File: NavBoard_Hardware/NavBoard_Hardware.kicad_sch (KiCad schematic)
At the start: 0 parts

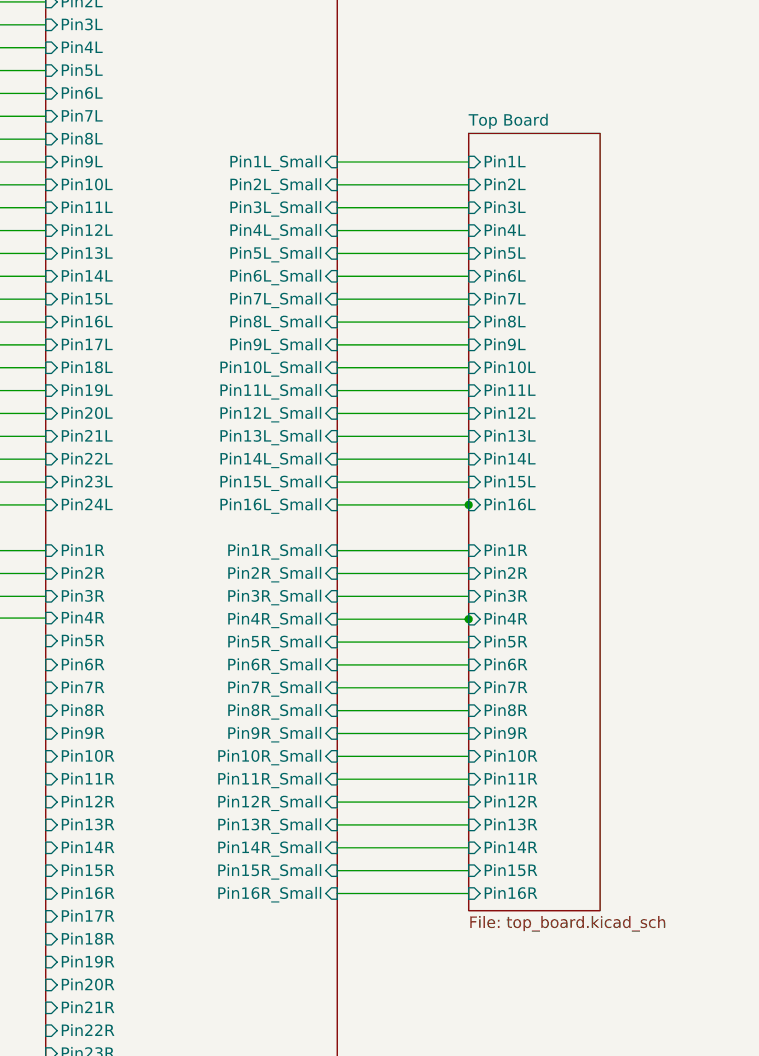
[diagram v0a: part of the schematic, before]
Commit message: Created adapter symbols and footprints
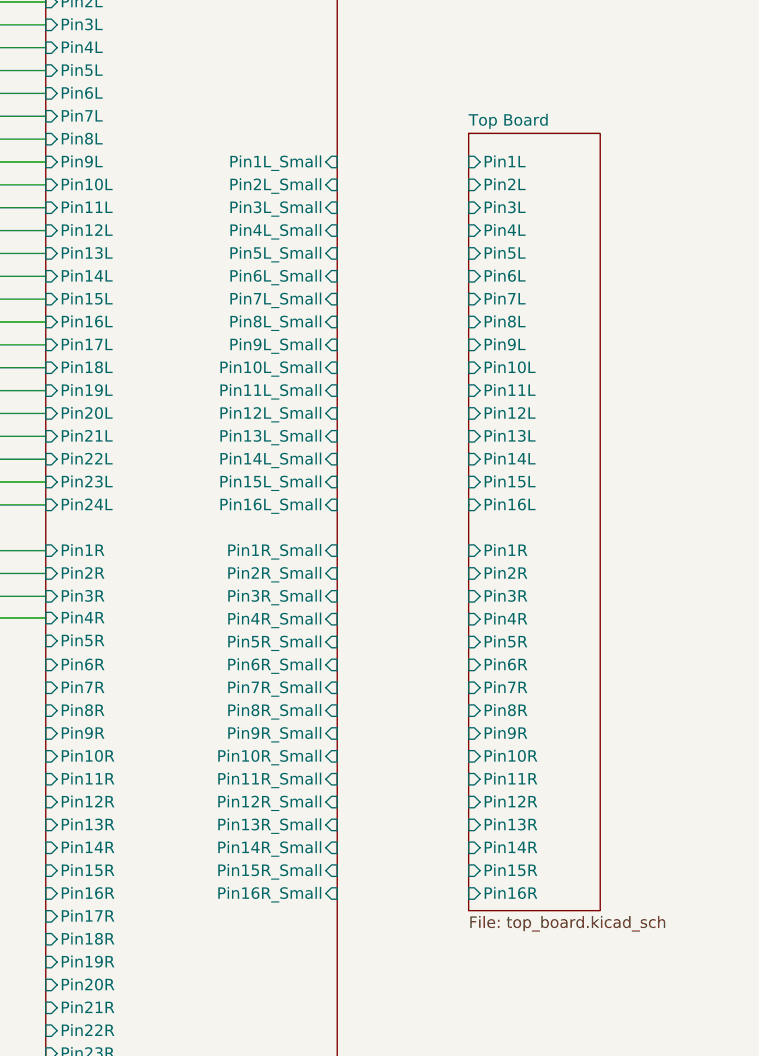
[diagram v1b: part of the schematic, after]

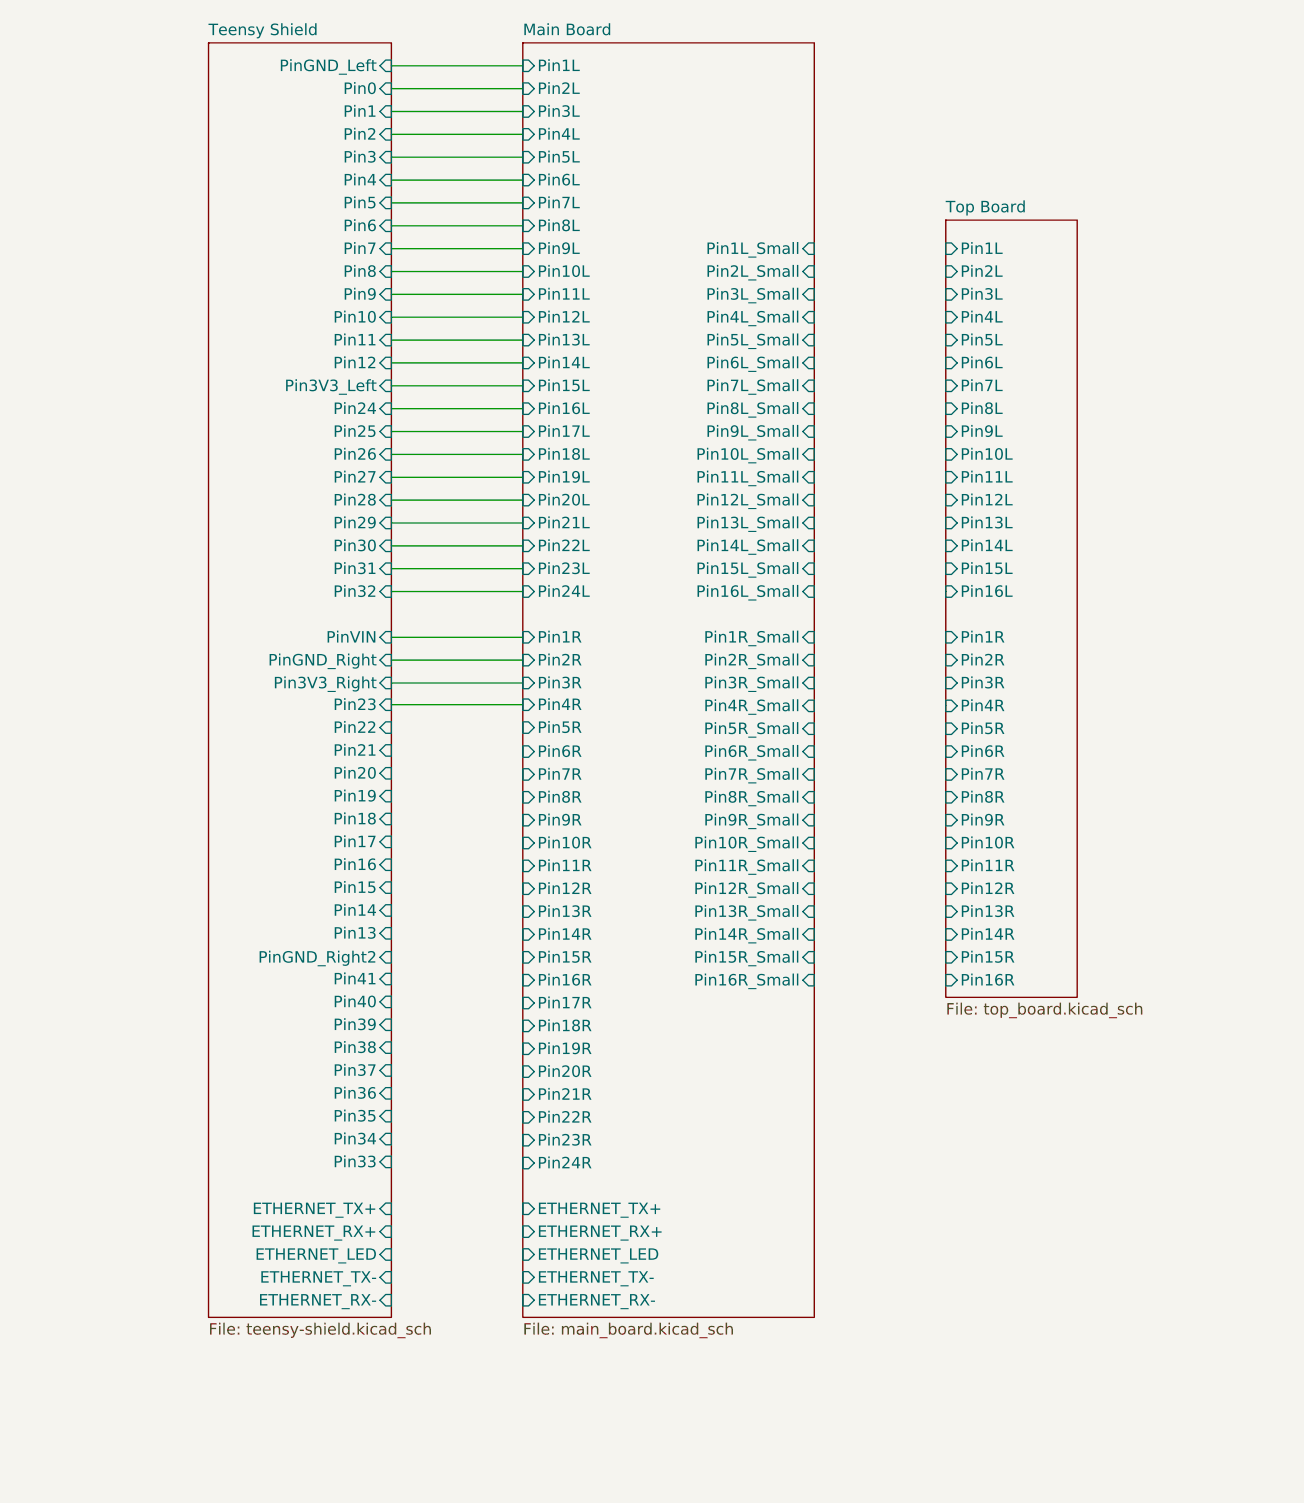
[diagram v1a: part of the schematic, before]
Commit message: Added connectors, cleaned up file directory
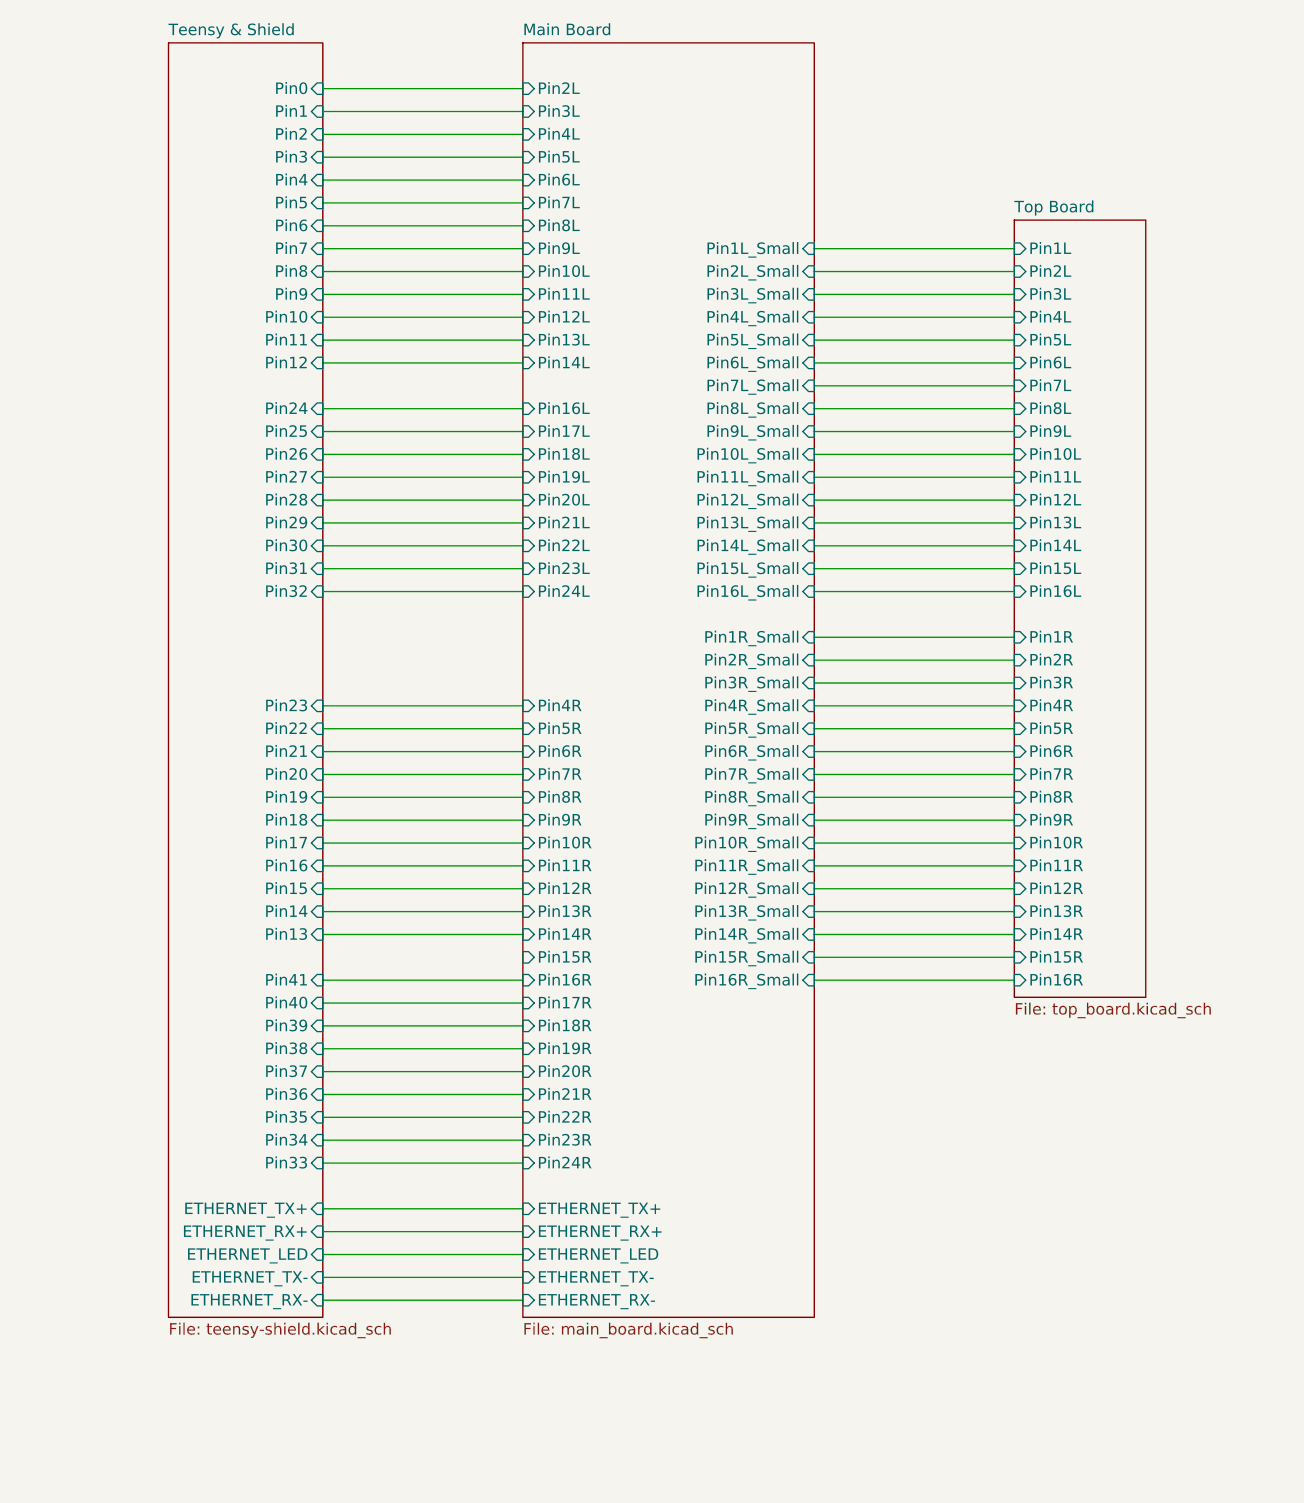
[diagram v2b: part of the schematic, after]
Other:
- removed sheet Teensy Shield
- added sheet Teensy & Shield (teensy-shield.kicad_sch)
- sheet Main Board ports: added none; removed Pin15L, Pin1L, Pin1R, Pin2R, Pin3R

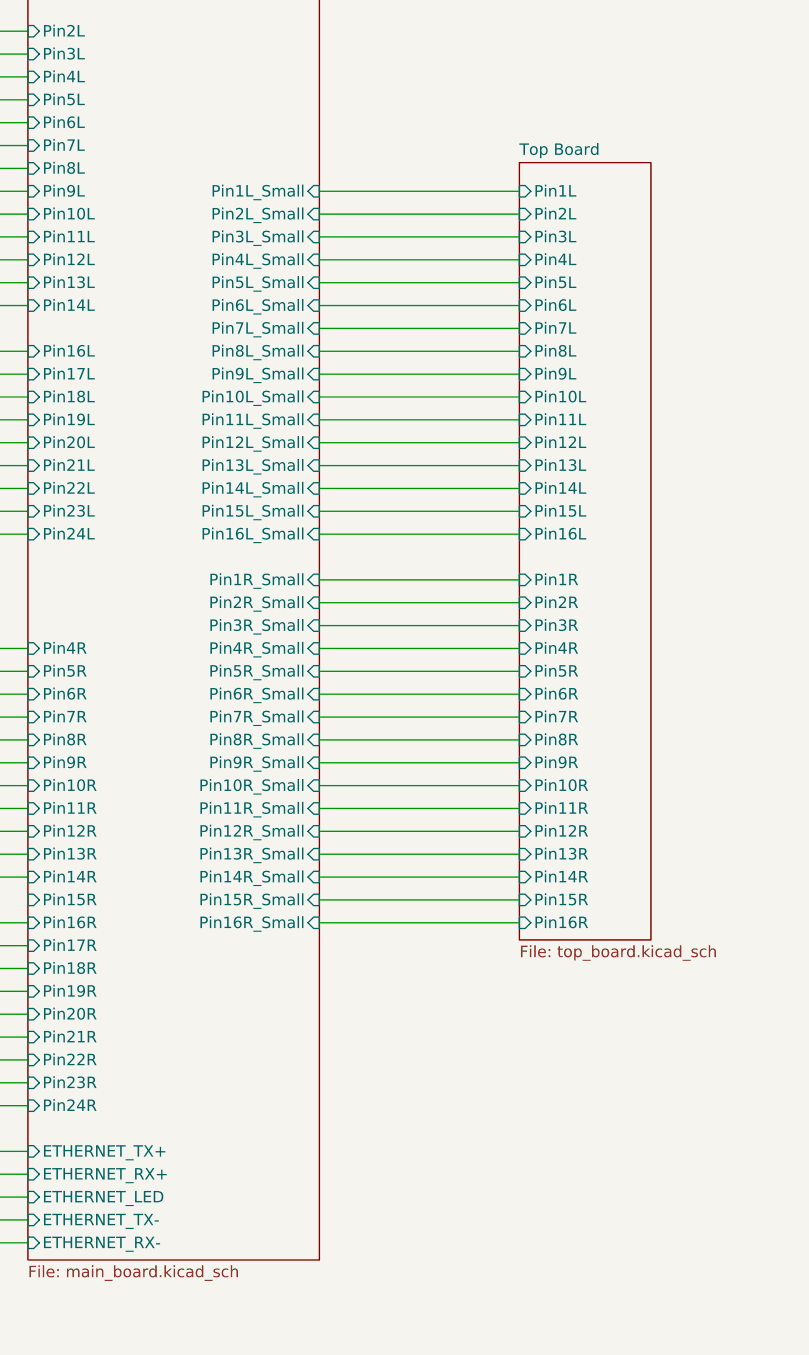
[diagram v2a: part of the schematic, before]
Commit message: Updated BMI component sheet from Navboard_2023_rev2
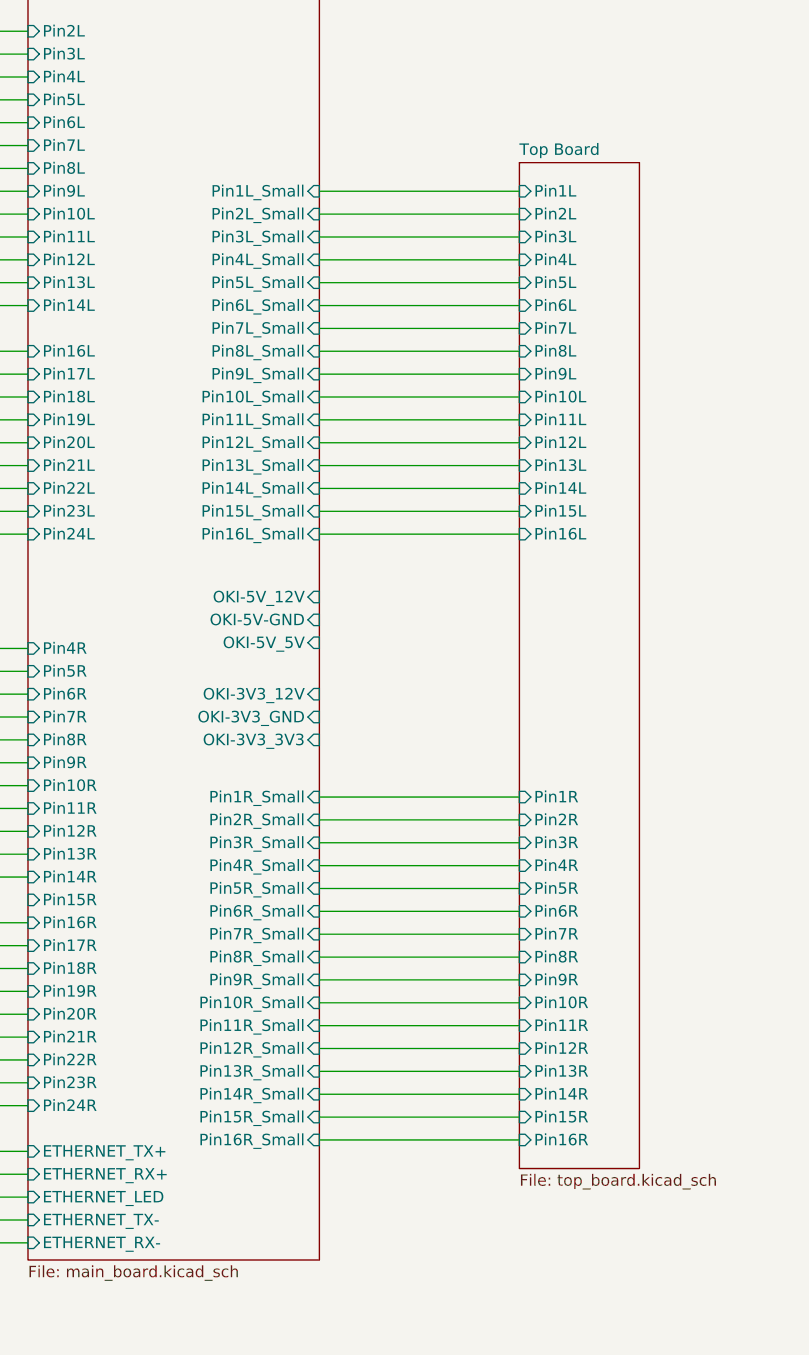
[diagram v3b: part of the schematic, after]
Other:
- sheet Main Board ports: added OKI-3V3_12V, OKI-3V3_3V3, OKI-3V3_GND, OKI-5V-GND, OKI-5V_12V, OKI-5V_5V; removed none
